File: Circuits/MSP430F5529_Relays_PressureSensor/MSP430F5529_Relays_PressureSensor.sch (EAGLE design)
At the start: 8 parts, among them K1 AQV21SMD, K2 AQV21SMD, U1 SSCDANT030PG2A3

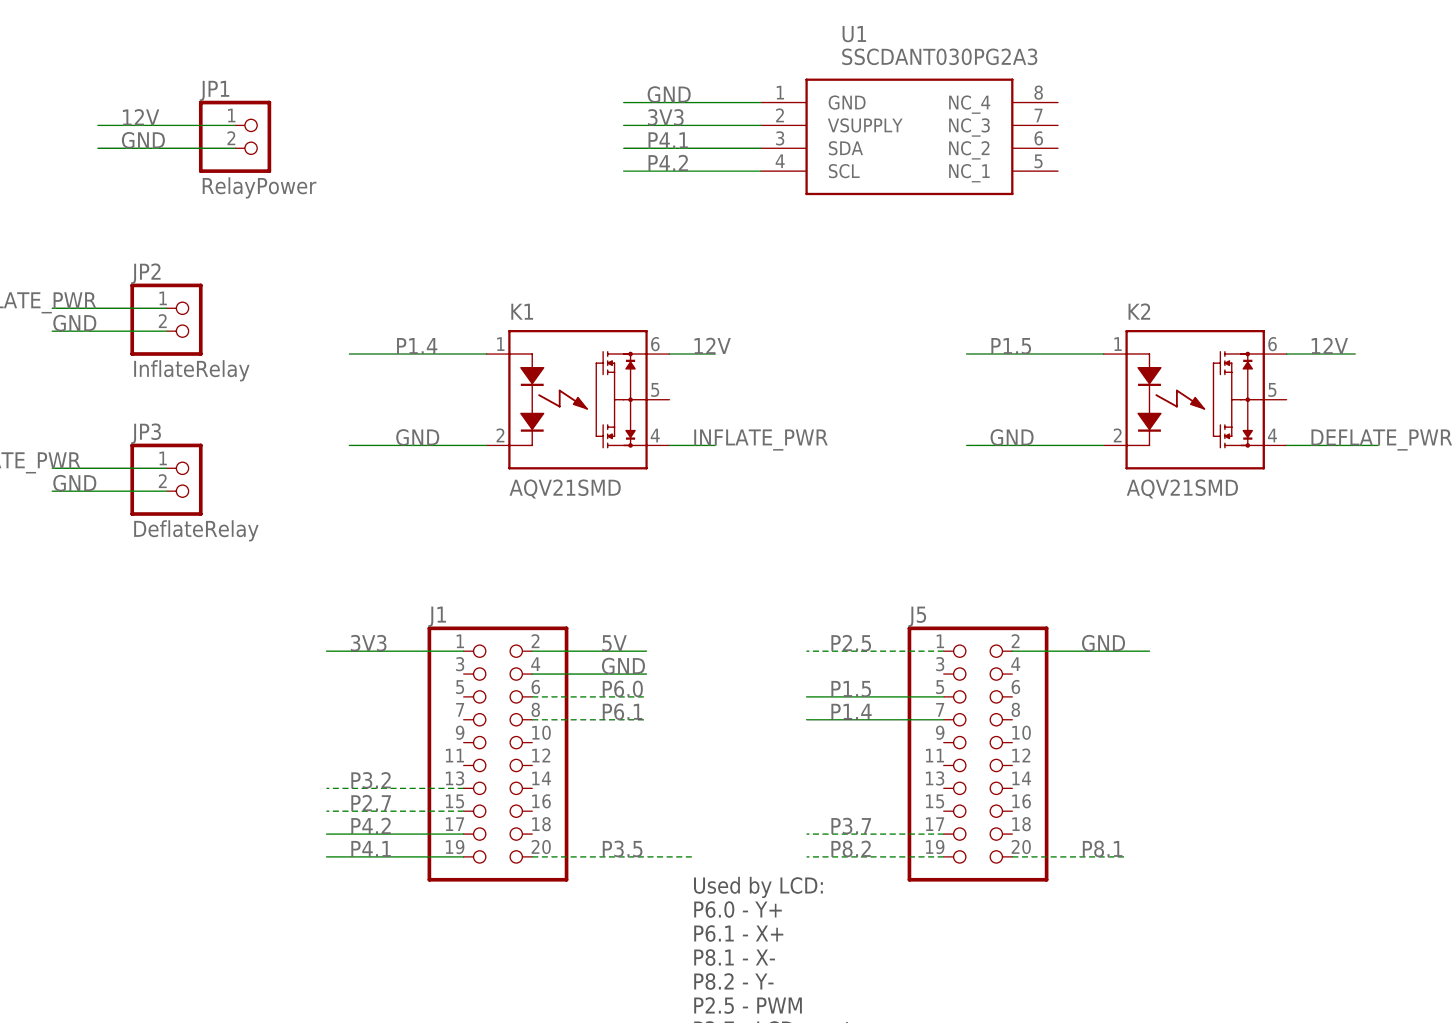
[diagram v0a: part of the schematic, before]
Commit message: add pullup resistors to I2C lines
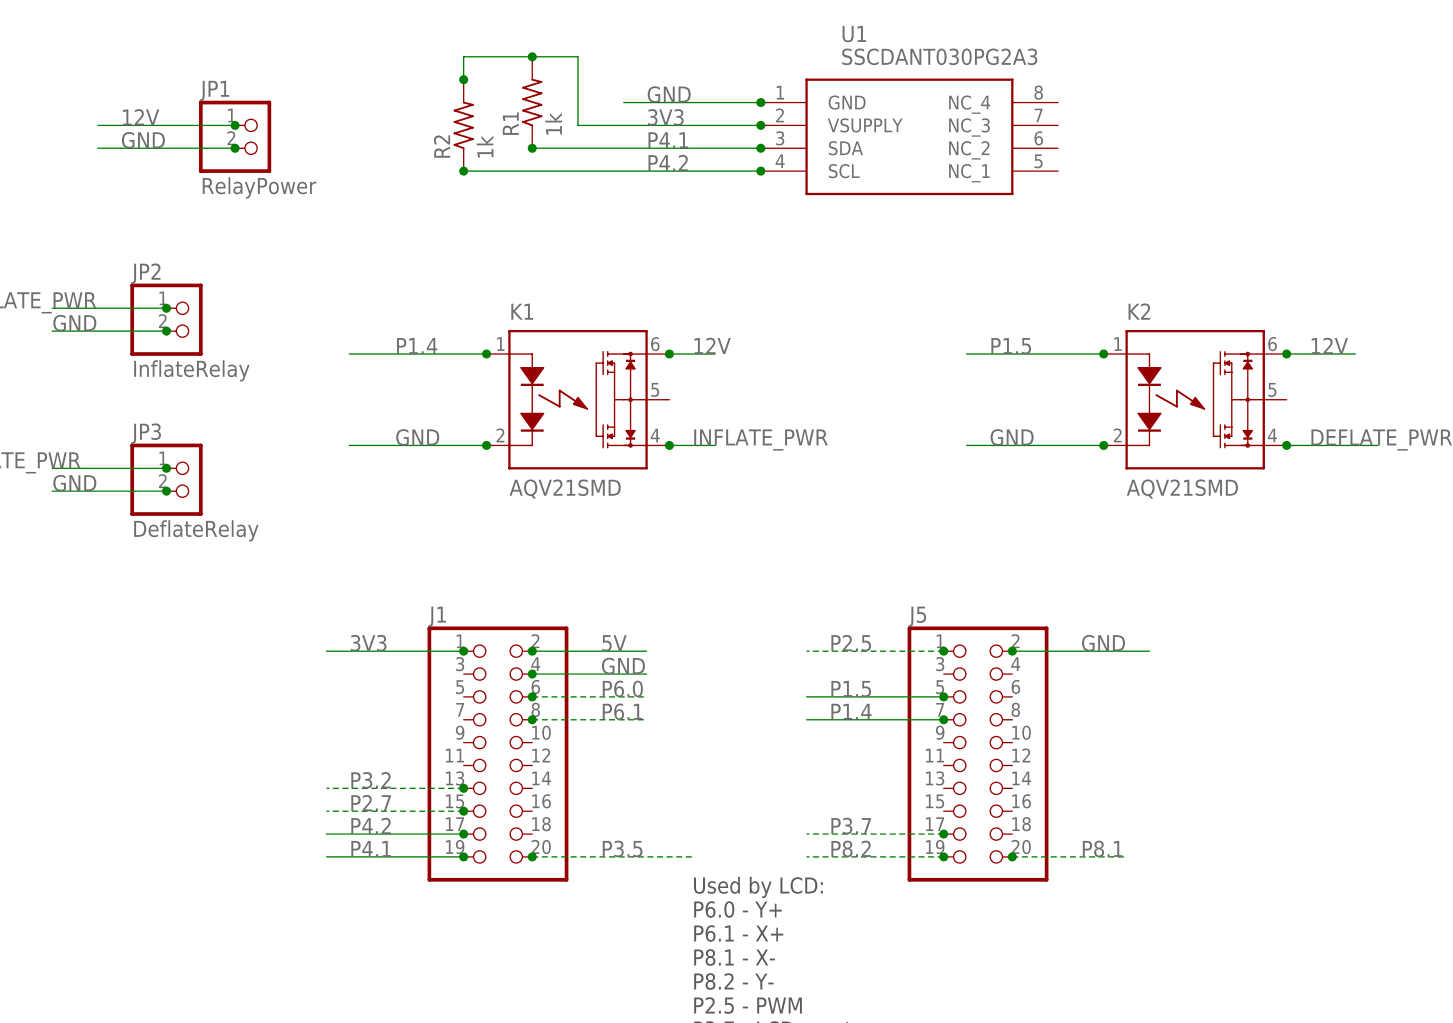
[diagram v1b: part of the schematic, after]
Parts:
- added R1, R2: 1k, resistor:R-US_M1206
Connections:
- net 3V3: now also R1.2, R2.2
- net P4.1: now also R1.1
- net P4.2: now also R2.1
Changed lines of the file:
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@@
 <layer number="97" name="Info" color="7" fill="1" visible="yes" active="yes"/>
 <layer number="98" name="Guide" color="6" fill="1" visible="yes" active="yes"/>
+<layer number="99" name="SpiceOrder" color="5" fill="1" visible="yes" active="yes"/>
 </layers>
 <schematic xreflabel="%F%N/%S.%C%R" xrefpart="/%S.%C%R">
@@
 <part name="JP2" library="pinhead" library_urn="urn:adsk.eagle:library:325" deviceset="PINHD-1X2" device="/90" package3d_urn="urn:adsk.eagle:package:22437/2" value="InflateRelay"/>
 <part name="JP3" library="pinhead" library_urn="urn:adsk.eagle:library:325" deviceset="PINHD-1X2" device="/90" package3d_urn="urn:adsk.eagle:package:22437/2" value="DeflateRelay"/>
+<part name="R1" library="resistor" library_urn="urn:adsk.eagle:library:348" deviceset="R-US_" device="M1206" package3d_urn="urn:adsk.eagle:package:26088/1" value="1k"/>
+<part name="R2" library="resistor" library_urn="urn:adsk.eagle:library:348" deviceset="R-US_" device="M1206" package3d_urn="urn:adsk.eagle:package:26088/1" value="1k"/>
 </parts>
 <sheets>
@@
 <attribute name="VALUE" x="-3.81" y="38.1" size="1.778" layer="96"/>
 </instance>
+<instance part="R1" gate="G$1" x="40.64" y="86.36" smashed="yes" rot="R90">
+<attribute name="NAME" x="39.1414" y="82.55" size="1.778" layer="95" rot="R90"/>
+<attribute name="VALUE" x="43.942" y="82.55" size="1.778" layer="96" rot="R90"/>
+</instance>
+<instance part="R2" gate="G$1" x="33.02" y="83.82" smashed="yes" rot="R90">
+<attribute name="NAME" x="31.5214" y="80.01" size="1.778" layer="95" rot="R90"/>
+<attribute name="VALUE" x="36.322" y="80.01" size="1.778" layer="96" rot="R90"/>
+</instance>
 </instances>
 <busses>
@@
 <wire x1="33.02" y1="25.4" x2="17.78" y2="25.4" width="0.1524" layer="91"/>
 <label x="20.32" y="25.4" size="1.778" layer="95"/>
+<junction x="33.02" y="25.4"/>
 </segment>
 <segment>
 <pinref part="U1" gate="G$1" pin="VSUPPLY"/>
-<wire x1="66.04" y1="83.82" x2="50.8" y2="83.82" width="0.1524" layer="91"/>
+<wire x1="66.04" y1="83.82" x2="45.72" y2="83.82" width="0.1524" layer="91"/>
 <label x="53.34" y="83.82" size="1.778" layer="95"/>
+<wire x1="45.72" y1="83.82" x2="45.72" y2="91.44" width="0.1524" layer="91"/>
+<pinref part="R2" gate="G$1" pin="2"/>
+<wire x1="33.02" y1="88.9" x2="33.02" y2="91.44" width="0.1524" layer="91"/>
+<pinref part="R1" gate="G$1" pin="2"/>
+<wire x1="33.02" y1="91.44" x2="40.64" y2="91.44" width="0.1524" layer="91"/>
+<wire x1="45.72" y1="91.44" x2="40.64" y2="91.44" width="0.1524" layer="91"/>
+<junction x="40.64" y="91.44"/>
+<junction x="33.02" y="88.9"/>
+<junction x="66.04" y="83.82"/>
 </segment>
 </net>
@@
 <wire x1="40.64" y1="25.4" x2="53.34" y2="25.4" width="0.1524" layer="91"/>
 <label x="48.26" y="25.4" size="1.778" layer="95"/>
+<junction x="40.64" y="25.4"/>
 </segment>
 </net>
@@
 <wire x1="40.64" y1="22.86" x2="53.34" y2="22.86" width="0.1524" layer="91"/>
 <label x="48.26" y="22.86" size="1.778" layer="95"/>
+<junction x="40.64" y="22.86"/>
 </segment>
 <segment>
@@
 <wire x1="93.98" y1="25.4" x2="109.22" y2="25.4" width="0.1524" layer="91"/>
 <label x="101.6" y="25.4" size="1.778" layer="95"/>
+<junction x="93.98" y="25.4"/>
 </segment>
 <segment>
@@
 <wire x1="66.04" y1="86.36" x2="50.8" y2="86.36" width="0.1524" layer="91"/>
 <label x="53.34" y="86.36" size="1.778" layer="95"/>
+<junction x="66.04" y="86.36"/>
 </segment>
 <segment>
@@
 <wire x1="7.62" y1="81.28" x2="-7.62" y2="81.28" width="0.1524" layer="91"/>
 <label x="-5.08" y="81.28" size="1.778" layer="95"/>
+<junction x="7.62" y="81.28"/>
 </segment>
 <segment>
@@
 <wire x1="35.56" y1="48.26" x2="20.32" y2="48.26" width="0.1524" layer="91"/>
 <label x="25.4" y="48.26" size="1.778" layer="95"/>
+<junction x="35.56" y="48.26"/>
 </segment>
 <segment>
@@
 <wire x1="104.14" y1="48.26" x2="88.9" y2="48.26" width="0.1524" layer="91"/>
 <label x="91.44" y="48.26" size="1.778" layer="95"/>
+<junction x="104.14" y="48.26"/>
 </segment>
 <segment>
@@
 <wire x1="0" y1="60.96" x2="-12.7" y2="60.96" width="0.1524" layer="91"/>
 <label x="-12.7" y="60.96" size="1.778" layer="95"/>
+<junction x="0" y="60.96"/>
 </segment>
 <segment>
@@
 <wire x1="0" y1="43.18" x2="-12.7" y2="43.18" width="0.1524" layer="91"/>
 <label x="-12.7" y="43.18" size="1.778" layer="95"/>
+<junction x="0" y="43.18"/>
 </segment>
 </net>
@@
 <wire x1="33.02" y1="2.54" x2="17.78" y2="2.54" width="0.1524" layer="91"/>
 <label x="20.32" y="2.54" size="1.778" layer="95"/>
+<junction x="33.02" y="2.54"/>
 </segment>
 <segment>
 <pinref part="U1" gate="G$1" pin="SDA"/>
-<wire x1="66.04" y1="81.28" x2="50.8" y2="81.28" width="0.1524" layer="91"/>
+<wire x1="66.04" y1="81.28" x2="40.64" y2="81.28" width="0.1524" layer="91"/>
 <label x="53.34" y="81.28" size="1.778" layer="95"/>
+<pinref part="R1" gate="G$1" pin="1"/>
+<junction x="40.64" y="81.28"/>
+<junction x="66.04" y="81.28"/>
 </segment>
 </net>
@@
 <wire x1="40.64" y1="2.54" x2="58.42" y2="2.54" width="0.1524" layer="91" style="dashdot"/>
 <label x="48.26" y="2.54" size="1.778" layer="95"/>
+<junction x="40.64" y="2.54"/>
 </segment>
 </net>
@@
 <wire x1="7.62" y1="83.82" x2="-7.62" y2="83.82" width="0.1524" layer="91"/>
 <label x="-5.08" y="83.82" size="1.778" layer="95"/>
+<junction x="7.62" y="83.82"/>
 </segment>
 <segment>
@@
 <wire x1="124.46" y1="58.42" x2="132.08" y2="58.42" width="0.1524" layer="91"/>
 <label x="127" y="58.42" size="1.778" layer="95"/>
+<junction x="124.46" y="58.42"/>
 </segment>
 <segment>
@@
 <wire x1="55.88" y1="58.42" x2="60.96" y2="58.42" width="0.1524" layer="91"/>
 <label x="58.42" y="58.42" size="1.778" layer="95"/>
+<junction x="55.88" y="58.42"/>
 </segment>
 </net>
@@
 <wire x1="33.02" y1="5.08" x2="17.78" y2="5.08" width="0.1524" layer="91"/>
 <label x="20.32" y="5.08" size="1.778" layer="95"/>
+<junction x="33.02" y="5.08"/>
 </segment>
 <segment>
 <pinref part="U1" gate="G$1" pin="SCL"/>
-<wire x1="66.04" y1="78.74" x2="50.8" y2="78.74" width="0.1524" layer="91"/>
 <label x="53.34" y="78.74" size="1.778" layer="95"/>
+<pinref part="R2" gate="G$1" pin="1"/>
+<wire x1="33.02" y1="78.74" x2="66.04" y2="78.74" width="0.1524" layer="91"/>
+<junction x="33.02" y="78.74"/>
+<junction x="66.04" y="78.74"/>
 </segment>
 </net>
@@
 <wire x1="86.36" y1="2.54" x2="71.12" y2="2.54" width="0.1524" layer="91" style="dashdot"/>
 <label x="73.66" y="2.54" size="1.778" layer="95"/>
+<junction x="86.36" y="2.54"/>
 </segment>
 </net>
@@
 <wire x1="93.98" y1="2.54" x2="106.68" y2="2.54" width="0.1524" layer="91" style="dashdot"/>
 <label x="101.6" y="2.54" size="1.778" layer="95"/>
+<junction x="93.98" y="2.54"/>
 </segment>
 </net>
@@
 <wire x1="40.64" y1="20.32" x2="53.34" y2="20.32" width="0.1524" layer="91" style="dashdot"/>
 <label x="48.26" y="20.32" size="1.778" layer="95"/>
+<junction x="40.64" y="20.32"/>
 </segment>
 </net>
@@
 <wire x1="40.64" y1="17.78" x2="53.34" y2="17.78" width="0.1524" layer="91" style="dashdot"/>
 <label x="48.26" y="17.78" size="1.778" layer="95"/>
+<junction x="40.64" y="17.78"/>
 </segment>
 </net>
@@
 <wire x1="33.02" y1="7.62" x2="17.78" y2="7.62" width="0.1524" layer="91" style="dashdot"/>
 <label x="20.32" y="7.62" size="1.778" layer="95"/>
+<junction x="33.02" y="7.62"/>
 </segment>
 </net>
@@
 <wire x1="33.02" y1="10.16" x2="17.78" y2="10.16" width="0.1524" layer="91" style="dashdot"/>
 <label x="20.32" y="10.16" size="1.778" layer="95"/>
+<junction x="33.02" y="10.16"/>
 </segment>
 </net>
@@
 <wire x1="86.36" y1="25.4" x2="71.12" y2="25.4" width="0.1524" layer="91" style="dashdot"/>
 <label x="73.66" y="25.4" size="1.778" layer="95"/>
+<junction x="86.36" y="25.4"/>
 </segment>
 </net>
@@
 <wire x1="86.36" y1="20.32" x2="71.12" y2="20.32" width="0.1524" layer="91"/>
 <label x="73.66" y="20.32" size="1.778" layer="95"/>
+<junction x="86.36" y="20.32"/>
 </segment>
 <segment>
@@
 <wire x1="104.14" y1="58.42" x2="88.9" y2="58.42" width="0.1524" layer="91"/>
 <label x="91.44" y="58.42" size="1.778" layer="95"/>
+<junction x="104.14" y="58.42"/>
 </segment>
 </net>
@@
 <wire x1="86.36" y1="17.78" x2="71.12" y2="17.78" width="0.1524" layer="91"/>
 <label x="73.66" y="17.78" size="1.778" layer="95"/>
+<junction x="86.36" y="17.78"/>
 </segment>
 <segment>
@@
 <wire x1="35.56" y1="58.42" x2="20.32" y2="58.42" width="0.1524" layer="91"/>
 <label x="25.4" y="58.42" size="1.778" layer="95"/>
+<junction x="35.56" y="58.42"/>
 </segment>
 </net>
@@
 <wire x1="86.36" y1="5.08" x2="71.12" y2="5.08" width="0.1524" layer="91" style="dashdot"/>
 <label x="73.66" y="5.08" size="1.778" layer="95"/>
+<junction x="86.36" y="5.08"/>
 </segment>
 </net>
@@
 <wire x1="0" y1="63.5" x2="-12.7" y2="63.5" width="0.1524" layer="91"/>
 <label x="-22.86" y="63.5" size="1.778" layer="95"/>
+<junction x="0" y="63.5"/>
 </segment>
 <segment>
@@
 <wire x1="55.88" y1="48.26" x2="60.96" y2="48.26" width="0.1524" layer="91"/>
 <label x="58.42" y="48.26" size="1.778" layer="95"/>
+<junction x="55.88" y="48.26"/>
 </segment>
 </net>
@@
 <wire x1="0" y1="45.72" x2="-12.7" y2="45.72" width="0.1524" layer="91"/>
 <label x="-25.4" y="45.72" size="1.778" layer="95"/>
+<junction x="0" y="45.72"/>
 </segment>
 <segment>
 <pinref part="K2" gate="G$1" pin="D2"/>
+<label x="127" y="48.26" size="1.778" layer="95"/>
 <wire x1="124.46" y1="48.26" x2="134.62" y2="48.26" width="0.1524" layer="91"/>
-<label x="127" y="48.26" size="1.778" layer="95"/>
-</segment>
-</net>
+<junction x="124.46" y="48.26"/>
+</segment>
+</net>

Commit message: Substitute right angle pressure sensor
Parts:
- removed U1: SSCDANT030PG2A3, SamacSys_Parts:SSCDANT030PG2A3
- added U2: SSCMRNN015PA3A3, SamacSys_Parts:SSCMRNN015PA3A3
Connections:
- net 3V3: now also U2.VSUPPLY; no longer U1.VSUPPLY
- net GND: now also U2.GND; no longer U1.GND
- net P4.1: now also U2.SDA; no longer U1.SDA
- net P4.2: now also U2.SCL; no longer U1.SCL
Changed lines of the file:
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@@
 <part name="K1" library="relay" library_urn="urn:adsk.eagle:library:339" deviceset="AQV*" device="SMD" package3d_urn="urn:adsk.eagle:package:24363/1" technology="21"/>
 <part name="K2" library="relay" library_urn="urn:adsk.eagle:library:339" deviceset="AQV*" device="SMD" package3d_urn="urn:adsk.eagle:package:24363/1" technology="21"/>
-<part name="U1" library="SamacSys_Parts" deviceset="SSCDANT030PG2A3" device=""/>
 <part name="J1" library="pinhead" library_urn="urn:adsk.eagle:library:325" deviceset="PINHD-2X10" device="" package3d_urn="urn:adsk.eagle:package:22405/2"/>
 <part name="J5" library="pinhead" library_urn="urn:adsk.eagle:library:325" deviceset="PINHD-2X10" device="" package3d_urn="urn:adsk.eagle:package:22405/2"/>
@@
 <part name="R1" library="resistor" library_urn="urn:adsk.eagle:library:348" deviceset="R-US_" device="M1206" package3d_urn="urn:adsk.eagle:package:26088/1" value="1k"/>
 <part name="R2" library="resistor" library_urn="urn:adsk.eagle:library:348" deviceset="R-US_" device="M1206" package3d_urn="urn:adsk.eagle:package:26088/1" value="1k"/>
+<part name="U2" library="SamacSys_Parts" deviceset="SSCMRNN015PA3A3" device=""/>
 </parts>
 <sheets>
@@
 <attribute name="VALUE" x="106.68" y="42.672" size="1.778" layer="96" font="vector"/>
 </instance>
-<instance part="U1" gate="G$1" x="66.04" y="86.36" smashed="yes">
-<attribute name="NAME" x="74.93" y="93.98" size="1.778" layer="95" align="center-left"/>
-<attribute name="VALUE" x="74.93" y="91.44" size="1.778" layer="96" align="center-left"/>
-</instance>
 <instance part="J1" gate="A" x="35.56" y="15.24" smashed="yes">
 <attribute name="NAME" x="29.21" y="28.575" size="1.778" layer="95"/>
@@
 <attribute name="NAME" x="31.5214" y="80.01" size="1.778" layer="95" rot="R90"/>
 <attribute name="VALUE" x="36.322" y="80.01" size="1.778" layer="96" rot="R90"/>
+</instance>
+<instance part="U2" gate="G$1" x="66.04" y="86.36" smashed="yes">
+<attribute name="NAME" x="95.25" y="93.98" size="1.778" layer="95" align="center-left"/>
+<attribute name="VALUE" x="95.25" y="91.44" size="1.778" layer="96" align="center-left"/>
 </instance>
 </instances>
@@
 </segment>
 <segment>
-<pinref part="U1" gate="G$1" pin="VSUPPLY"/>
+<label x="53.34" y="83.82" size="1.778" layer="95"/>
 <wire x1="66.04" y1="83.82" x2="45.72" y2="83.82" width="0.1524" layer="91"/>
-<label x="53.34" y="83.82" size="1.778" layer="95"/>
 <wire x1="45.72" y1="83.82" x2="45.72" y2="91.44" width="0.1524" layer="91"/>
 <pinref part="R2" gate="G$1" pin="2"/>
@@
 <junction x="40.64" y="91.44"/>
 <junction x="33.02" y="88.9"/>
+<pinref part="U2" gate="G$1" pin="VSUPPLY"/>
 <junction x="66.04" y="83.82"/>
 </segment>
@@
 </segment>
 <segment>
-<pinref part="U1" gate="G$1" pin="GND"/>
 <wire x1="66.04" y1="86.36" x2="50.8" y2="86.36" width="0.1524" layer="91"/>
 <label x="53.34" y="86.36" size="1.778" layer="95"/>
+<pinref part="U2" gate="G$1" pin="GND"/>
 <junction x="66.04" y="86.36"/>
 </segment>
@@
 </segment>
 <segment>
-<pinref part="U1" gate="G$1" pin="SDA"/>
 <wire x1="66.04" y1="81.28" x2="40.64" y2="81.28" width="0.1524" layer="91"/>
 <label x="53.34" y="81.28" size="1.778" layer="95"/>
 <pinref part="R1" gate="G$1" pin="1"/>
 <junction x="40.64" y="81.28"/>
+<pinref part="U2" gate="G$1" pin="SDA"/>
 <junction x="66.04" y="81.28"/>
 </segment>
@@
 </segment>
 <segment>
-<pinref part="U1" gate="G$1" pin="SCL"/>
 <label x="53.34" y="78.74" size="1.778" layer="95"/>
 <pinref part="R2" gate="G$1" pin="1"/>
 <wire x1="33.02" y1="78.74" x2="66.04" y2="78.74" width="0.1524" layer="91"/>
 <junction x="33.02" y="78.74"/>
+<pinref part="U2" gate="G$1" pin="SCL"/>
 <junction x="66.04" y="78.74"/>
 </segment>
